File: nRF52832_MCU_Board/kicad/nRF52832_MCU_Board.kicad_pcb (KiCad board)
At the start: 2 copper layers, 65 x 40 mm, 60 parts, among them J1 CONN_01X03, J2 CONN_01X16, J3 CONN_01X08, J4 CONN_01X03, J5 MICROUSB, J6 CONN_02X05, J7 CONN_01X05, J8 MM8130-2600, J9 CONN_01X08, SW1 SW_SPST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

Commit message: Update KiCAD Project nRF52832_MCU_Board
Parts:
- BATT1: value CR1632 -> CR2032; footprint w_battery_holders:keystone_3000 -> Nordic_misc:keystone_3003
- moved R12 10.3 mm to (52.0, 98.7), turned to 180 degrees
- moved MK1 10.1 mm to (48.5, 118.0)
- moved D1 10.0 mm to (53.8, 100.2)
- moved J5 10.0 mm to (47.3, 99.9)
- moved MK4 10.0 mm to (48.5, 83.5), turned to 180 degrees
- moved R9 10.0 mm to (52.2, 102.3)
- moved J1 9.34 mm to (60.8, 118.0)
- moved C16 9.26 mm to (77.9, 93.9), turned to 180 degrees
- moved C18 7.60 mm to (76.4, 101.8), turned to 270 degrees
- moved R13 7.56 mm to (76.6, 99.2), turned to 270 degrees
- moved U2 6.93 mm to (81.7, 99.6)
- moved BATT1 5.81 mm to (55.1, 100.0)
- moved C17 4.91 mm to (77.9, 95.2), turned to 180 degrees
- moved C19 4.33 mm to (84.1, 104.3), turned to 180 degrees
- moved C14 2.54 mm to (91.7, 105.0)
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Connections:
- J5 pad 2: (no net) -> Net-(J5-Pad2)
- J5 pad 3: (no net) -> Net-(J5-Pad3)
- J5 pad 4: (no net) -> Net-(J5-Pad4)
- J6 pad 4: (no net) -> Net-(J6-Pad4)
- J6 pad 7: (no net) -> Net-(J6-Pad7)
- J6 pad 8: (no net) -> Net-(J6-Pad8)
- J7 pad 1: (no net) -> Net-(J7-Pad1)
- J7 pad 3: (no net) -> Net-(J7-Pad3)
- J7 pad 5: (no net) -> Net-(J7-Pad5)
- nRF1 pad 44: (no net) -> Net-(nRF1-Pad44)
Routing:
- net GND: track 276.5 -> 378.4 mm
- net +5V: track 44.4 -> 68.2 mm
- net +3.3VP: track 7.75 -> 21.6 mm
- net +3V3: track 125.6 -> 136.5 mm, vias 9 -> 6
- net /P0.10: track 37.1 -> 30.3 mm
- net /P0.09: track 36.8 -> 34.3 mm
- net /P0.07: track 35.6 -> 33.3 mm
- net /nRF528323_MCU/NFC2: track 18.7 -> 20.7 mm
- net /P0.12: track 34.8 -> 36.4 mm
- net /P0.21: track 41.4 -> 43.0 mm
- net /P0.11: track 36.5 -> 38.0 mm
- net /P0.08: track 39.5 -> 38.0 mm
- net +5VD: track 3.08 -> 1.63 mm
- net /P0.16: track 25.7 -> 26.8 mm
- net /P0.13: track 33.0 -> 34.1 mm
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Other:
- board size 65 x 40 mm -> 76.5 x 41.5 mm

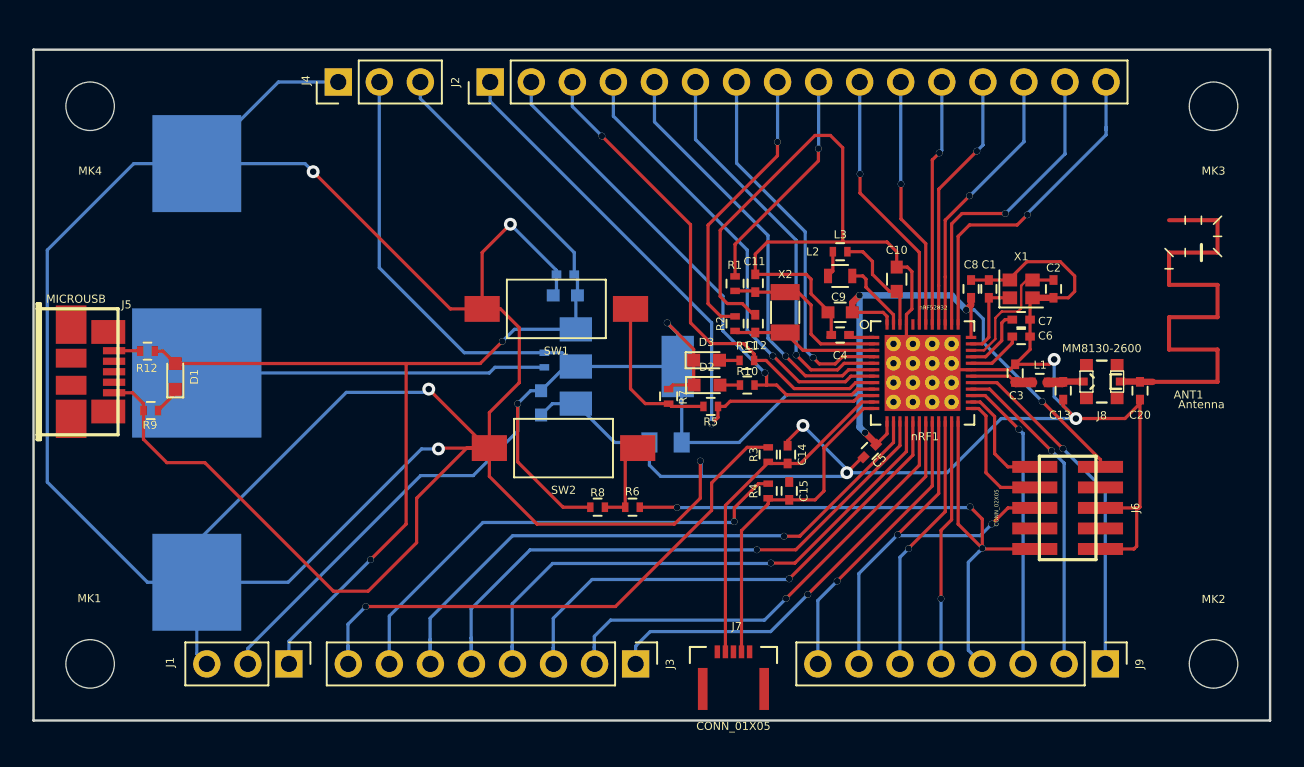
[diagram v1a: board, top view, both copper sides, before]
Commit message: Update kicad-_pcb file of project nRF52832_MCU_Board
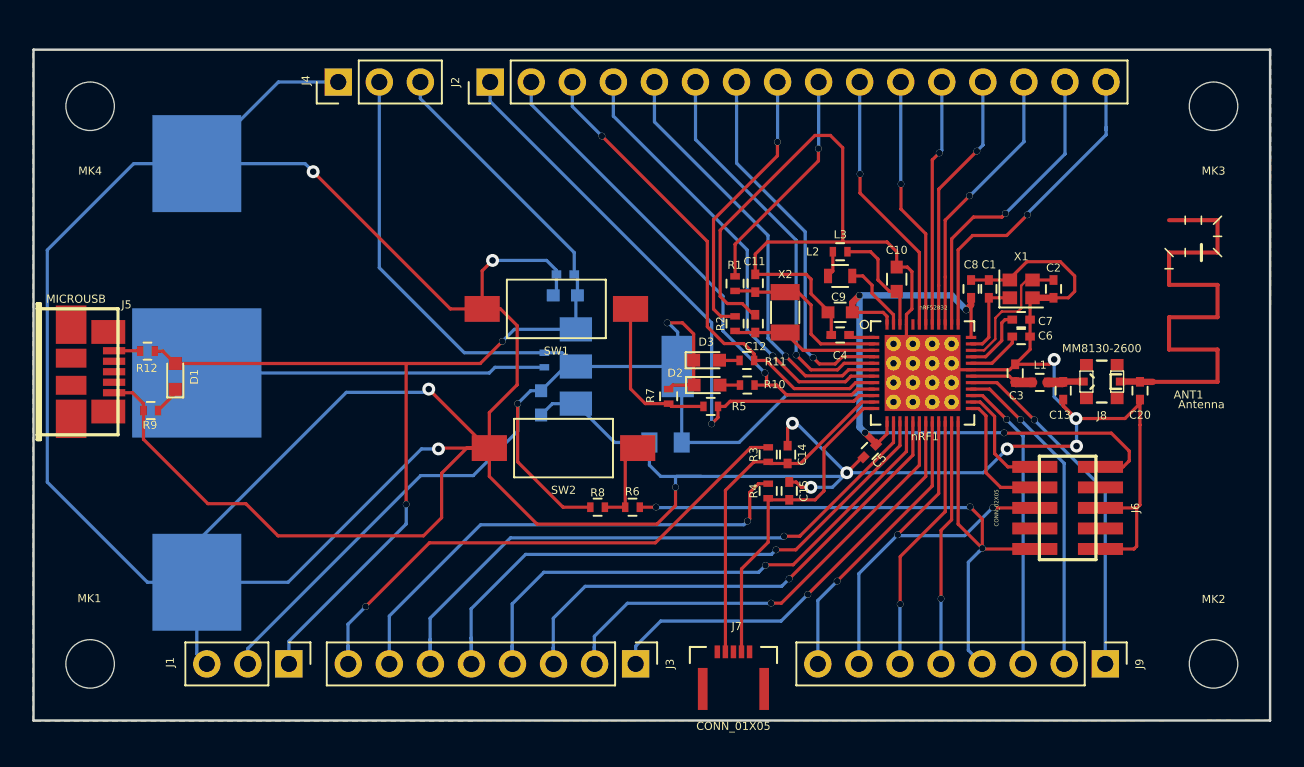
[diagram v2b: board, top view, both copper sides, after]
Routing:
- net +3V3: track 136.5 -> 143.0 mm
- net /P0.09: track 34.3 -> 33.3 mm
- net GND: track 378.4 -> 377.8 mm, vias 9 -> 12
- net /P0.26: track 19.5 -> 18.9 mm
- net /nRF528323_MCU/NFC1: track 21.0 -> 21.5 mm
- added copper zone on B.Cu, net GND
- added copper zone on F.Cu, net GND

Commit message: Update project nRF52832_MCU_Board
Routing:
- net GND: track 377.8 -> 343.4 mm
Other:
- net class Default: clearance 0.15 -> 0
- rule trace_clearance: 0.15 -> 0

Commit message: Update minors trace changes
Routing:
- net GND: track 343.4 -> 346.2 mm

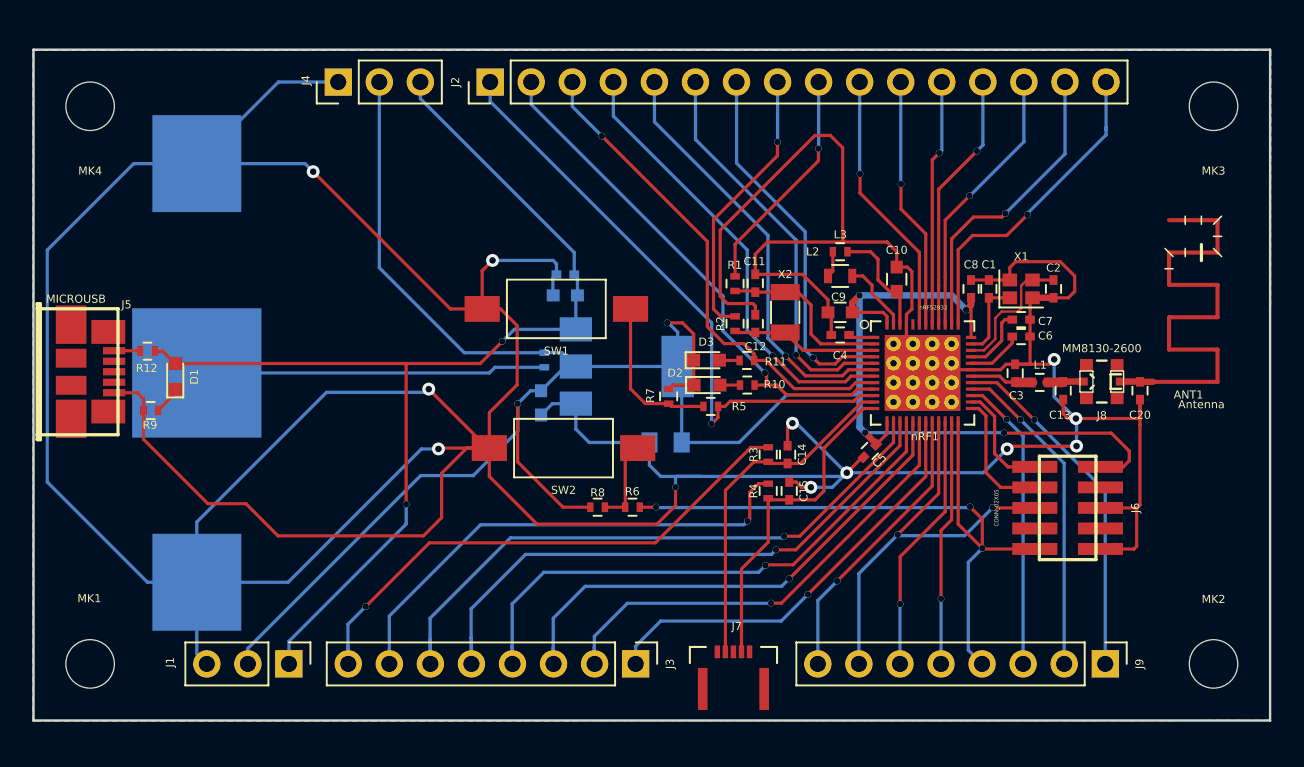
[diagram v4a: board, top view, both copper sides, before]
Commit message: Update nRF52832_MCU_Board
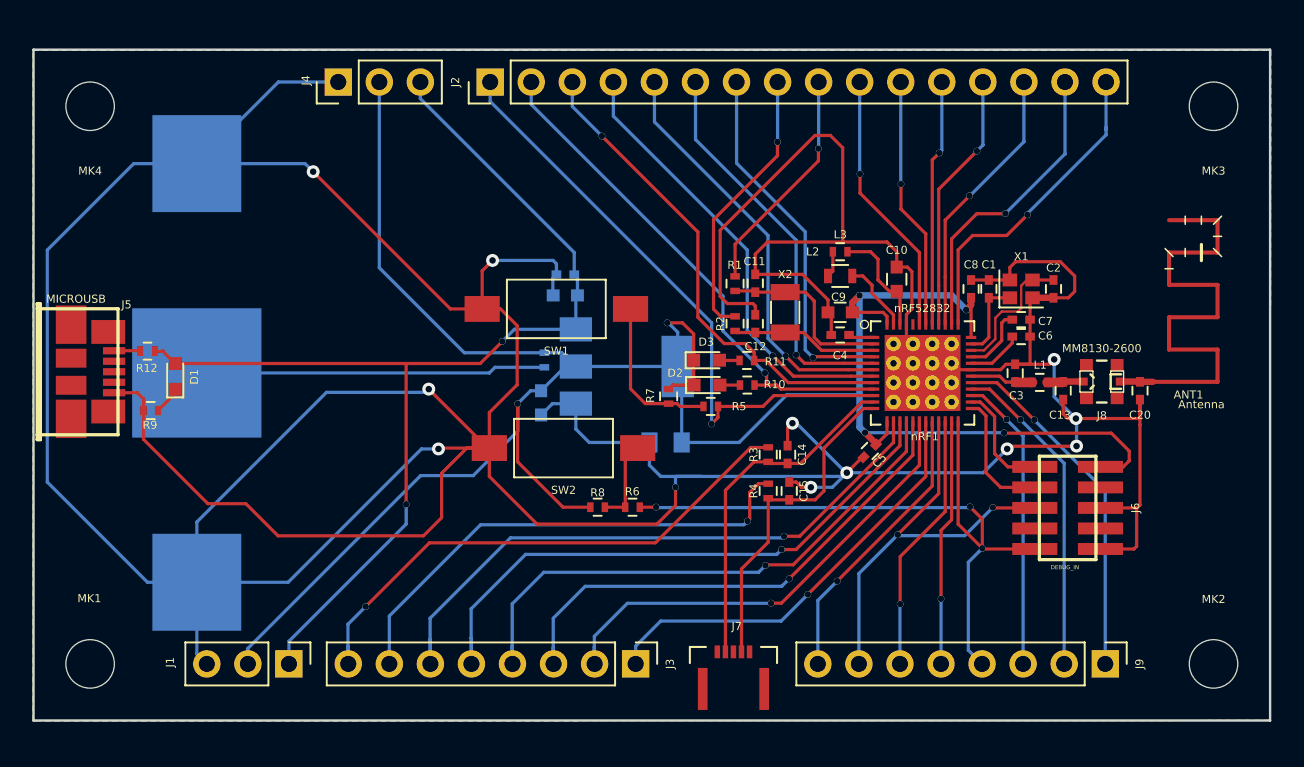
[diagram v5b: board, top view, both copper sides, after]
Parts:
- J6: value CONN_02X05 -> DEBUG_IN
- J7: value CONN_01X05 -> NFC
